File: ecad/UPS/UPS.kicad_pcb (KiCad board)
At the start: 4 copper layers, 177.8 x 139.7 mm, 162 parts, among them J1 Barrel_Jack, J2 Conn_01x02_Pin, J3 USB_C_Receptacle_USB2.0_16P, J4 PROG, J5 Conn_01x02_Pin, J6 Conn_01x02_Pin, Q1 CSD18540Q5B, Q2 Q_PMOS_DGS, Q3 IRLR7843TRPBF, Q4 Q_PMOS_DGS, Q5 CSD18540Q5B, Q6 CSD18540Q5B, Q7 CSD18540Q5B, SW3 SW_DPDT_x2, U1 BQ25730RSNR, U2 MPQ5031GRE-0001-AEC1-P, U3 L78L05_SOT89, U4 STM32L152RCT6, U5 AP2112K-3.3TRG1, U6 BOOT0, U7 NRST

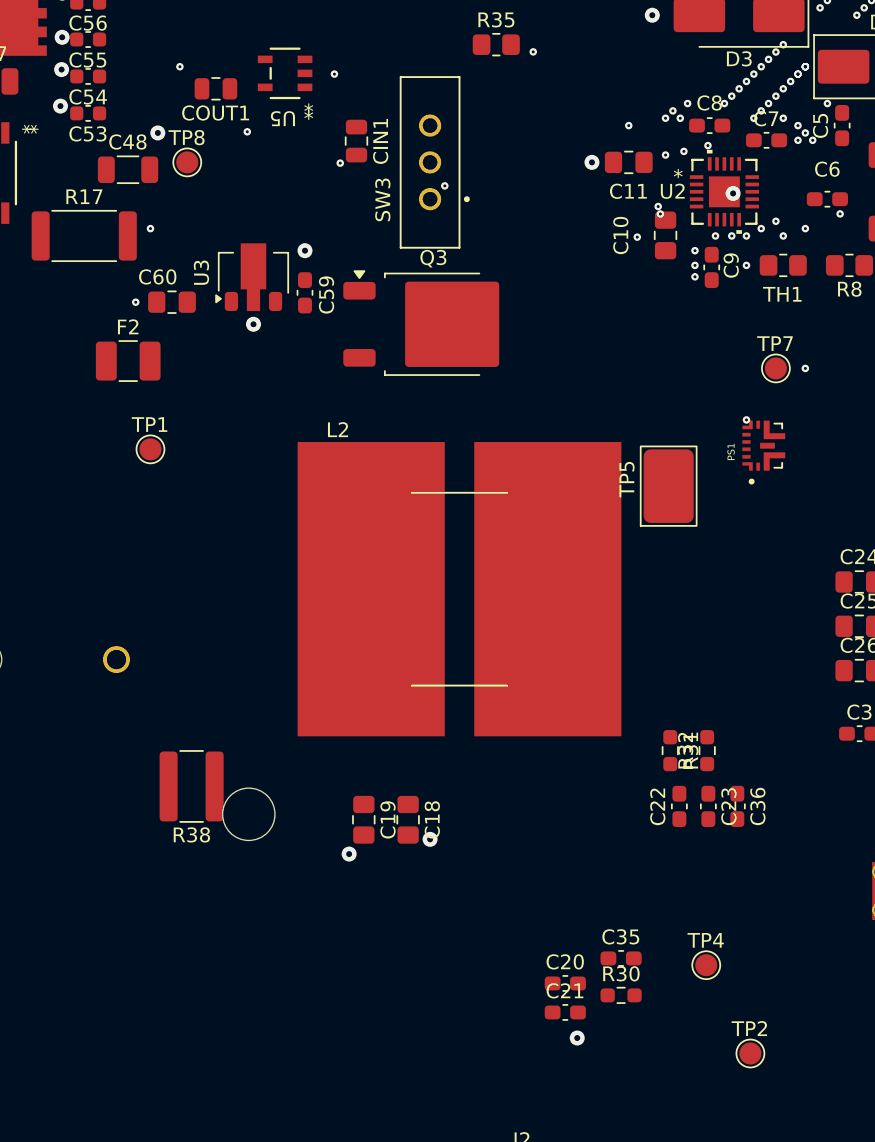
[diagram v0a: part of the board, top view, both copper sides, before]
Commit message: Final schematic, added fan, shrunk board down about 25%
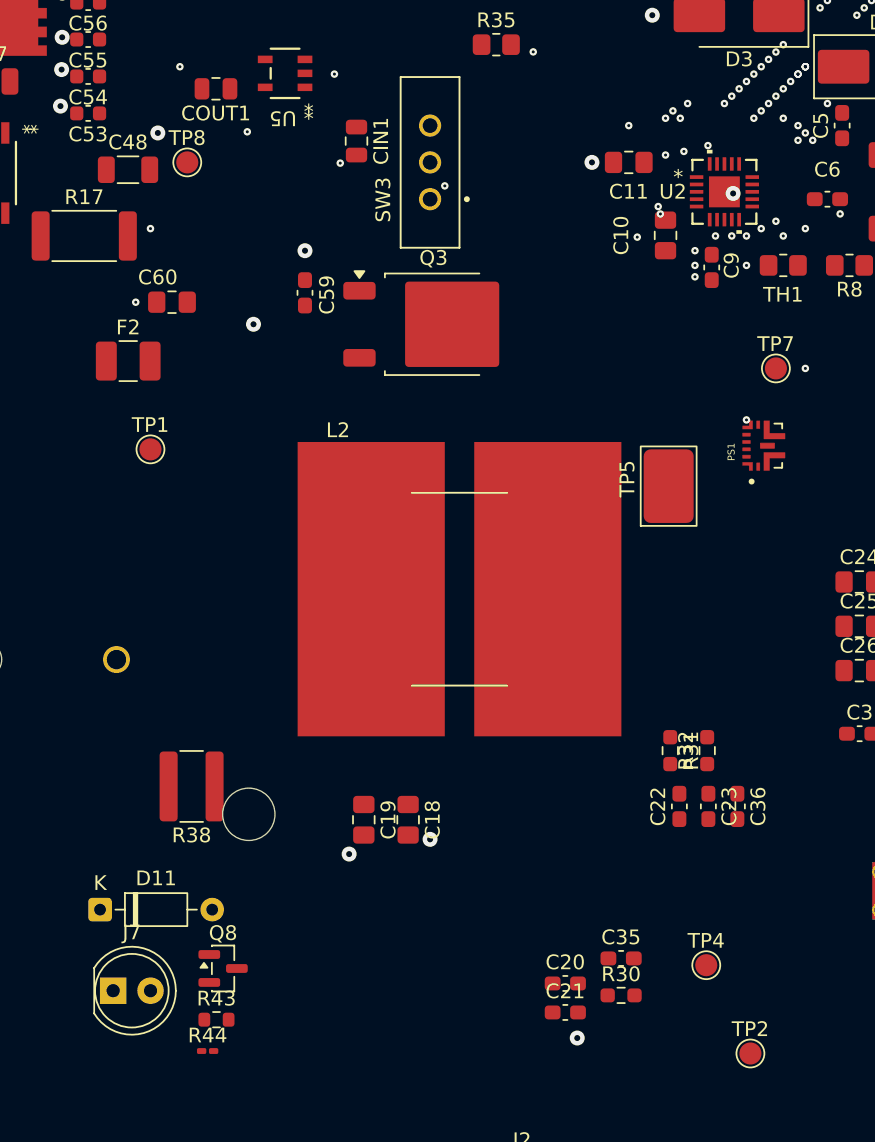
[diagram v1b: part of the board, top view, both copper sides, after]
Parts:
- removed C7, C8: 1nF, Capacitor_SMD:C_0603_1608Metric_Pad1.08x0.95mm_HandSolder
- removed U3: L78L05_SOT89, Package_TO_SOT_SMD:SOT-89-3
- added D11: 1N4148, Diode_THT:D_DO-35_SOD27_P7.62mm_Horizontal, F.Cu at (150.1, 111.8)
- added J7: Fan_Connector, LED_THT:LED_D5.0mm_IRGrey, F.Cu at (151.0, 117.3)
- added Q8: 2N7002, Package_TO_SOT_SMD:SOT-23, F.Cu at (158.4, 115.8)
- added R43: 100, Resistor_SMD:R_0603_1608Metric, F.Cu at (158.0, 119.3)
- added R44: 10K, Resistor_SMD:R_0201_0603Metric_Pad0.64x0.40mm_HandSolder, F.Cu at (157.4, 121.4)
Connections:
- C59 pad 1: /Output/VBUS_fused -> +5V
- F2 pad 2: /Output/VBUS_fused -> +5V
- Q3 pad 2: /Output/VBUS_out -> +5V
- Q3 pad 3: /Output/VBUS_fused -> /Output/VBUS_out
- U4 pad 26: unconnected-(U4B-PB0-Pad26) -> /controller/PB0
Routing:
- net PGND: vias 144 -> 148
- net Net-(U1-IADPT): vias 2 -> 1
- net NRST: vias 3 -> 1
- net GNDA: vias 11 -> 10

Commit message: ACTUALLY Shrunk board size haha
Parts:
- R40: footprint Resistor_SMD:R_0201_0603Metric_Pad0.64x0.40mm_HandSolder -> Resistor_SMD:R_0603_1608Metric_Pad0.98x0.95mm_HandSolder
- moved PS1 109.2 mm to (88.0, 101.0)
- moved L2 106.3 mm to (68.5, 82.0)
- moved C10 103.1 mm to (85.5, 70.0)
- moved C20 102.2 mm to (81.0, 99.0)
- moved U5 93.9 mm to (95.6, 120.7), turned to 0 degrees
- moved J7 85.7 mm to (65.2, 117.3)
- moved Q8 85.7 mm to (72.7, 115.8)
- moved R43 85.7 mm to (72.2, 119.3)
- moved D11 85.7 mm to (64.3, 111.8)
- moved R44 85.7 mm to (71.6, 121.4)
- moved C11 84.4 mm to (102.5, 73.0)
- moved SW3 78.8 mm to (94.5, 72.0)
- moved Q3 74.4 mm to (99.0, 82.3)
- moved C64 60.9 mm to (148.4, 116.0)
- moved R40 60.9 mm to (151.4, 114.0)
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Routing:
- net VDDA: vias 3 -> 0
- net PGND: vias 148 -> 0
- net Net-(U2-NTC): vias 2 -> 0
- net Net-(U1-SW2): vias 2 -> 0
- net Net-(U1-LODRV2): vias 2 -> 0
- net Net-(U1-IBAT): vias 2 -> 0
- net Net-(U1-IADPT): vias 1 -> 0
- net Net-(U1-ACN): vias 2 -> 0
- net Net-(SW3A-A): vias 2 -> 0
- net Net-(PS1-VIN): vias 2 -> 0
- net NRST: vias 1 -> 0
- net GNDA: vias 10 -> 0
- net COMP1: vias 1 -> 0
- net /Output/vsel2: vias 1 -> 0
- net /Output/SCL: vias 2 -> 0
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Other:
- board text added: "OSHE Pi UPS rev 2.0"
- board text removed: "OSHE Pi UPS rev 1.0"

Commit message: Started GND consolidation
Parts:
- moved C38 1.64 mm to (114.5, 85.5), turned to 90 degrees
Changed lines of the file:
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@@
 	(footprint "Capacitor_SMD:C_0603_1608Metric"
 		(layer "F.Cu")
-		(at 115.698301 84.378599)
+		(at 114.5 85.5 90)
 		(descr "Capacitor SMD 0603 (1608 Metric), square (rectangular) end terminal, IPC-7351 nominal, (Body size source: IPC-SM-782 page 76, https://www.pcb-3d.com/wordpress/wp-content/uploads/ipc-sm-782a_amendment_1_and_2.pdf), generated with kicad-footprint-generator")
 		(tags "capacitor")
 		(property "Reference" "C38"
-			(at 0 -1.43 0)
+			(at 0 -1.43 90)
 			(layer "F.SilkS")
 			(effects
@@
 		)
 		(property "Value" "1µF"
-			(at 0 1.43 0)
+			(at 0 1.43 90)
 			(layer "F.Fab")
 			(effects
@@
 		)
 		(property "Datasheet" ""
-			(at 0 0 0)
+			(at 0 0 90)
 			(layer "F.Fab")
 			(hide yes)
@@
 		)
 		(property "Description" "Unpolarized capacitor"
-			(at 0 0 0)
+			(at 0 0 90)
 			(layer "F.Fab")
 			(hide yes)
@@
 		)
 		(fp_line
+			(start 1.48 -0.73)
+			(end 1.48 0.73)
+			(stroke
+				(width 0.05)
+				(type solid)
+			)
+			(layer "F.CrtYd")
+		)
+		(fp_line
 			(start -1.48 -0.73)
 			(end 1.48 -0.73)
+			(stroke
+				(width 0.05)
+				(type solid)
+			)
+			(layer "F.CrtYd")
+		)
+		(fp_line
+			(start 1.48 0.73)
+			(end -1.48 0.73)
 			(stroke
 				(width 0.05)
@@
 		)
 		(fp_line
-			(start 1.48 -0.73)
-			(end 1.48 0.73)
+			(start 0.8 -0.4)
+			(end 0.8 0.4)
 			(stroke
-				(width 0.05)
+				(width 0.1)
 				(type solid)
 			)
-			(layer "F.CrtYd")
-		)
-		(fp_line
-			(start 1.48 0.73)
-			(end -1.48 0.73)
-			(stroke
-				(width 0.05)
-				(type solid)
-			)
-			(layer "F.CrtYd")
+			(layer "F.Fab")
 		)
 		(fp_line
 			(start -0.8 -0.4)
 			(end 0.8 -0.4)
+			(stroke
+				(width 0.1)
+				(type solid)
+			)
+			(layer "F.Fab")
+		)
+		(fp_line
+			(start 0.8 0.4)
+			(end -0.8 0.4)
 			(stroke
 				(width 0.1)
@@
 			(layer "F.Fab")
 		)
-		(fp_line
-			(start 0.8 -0.4)
-			(end 0.8 0.4)
-			(stroke
-				(width 0.1)
-				(type solid)
-			)
-			(layer "F.Fab")
-		)
-		(fp_line
-			(start 0.8 0.4)
-			(end -0.8 0.4)
-			(stroke
-				(width 0.1)
-				(type solid)
-			)
-			(layer "F.Fab")
-		)
 		(fp_text user "${REFERENCE}"
-			(at 0 0 0)
+			(at 0 0 90)
 			(layer "F.Fab")
 			(effects
@@
 		)
 		(pad "1" smd roundrect
-			(at -0.775 0)
+			(at -0.775 0 90)
 			(size 0.9 0.95)
 			(layers "F.Cu" "F.Mask" "F.Paste")
@@
 		)
 		(pad "2" smd roundrect
-			(at 0.775 0)
+			(at 0.775 0 90)
 			(size 0.9 0.95)
 			(layers "F.Cu" "F.Mask" "F.Paste")

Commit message: Update R41 Resistor from 0201 to 0603
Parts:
- R41: footprint Resistor_SMD:R_0201_0603Metric_Pad0.64x0.40mm_HandSolder -> Resistor_SMD:R_0603_1608Metric_Pad0.98x0.95mm_HandSolder
- TP3: value PGNDTest -> GNDTest
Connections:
- B1 pad 1: PGND -> GND
- B2 pad 1: PGND -> GND
- B3 pad 1: PGND -> GND
- B4 pad 1: PGND -> GND
- C1 pad 2: GNDA -> GND
- C10 pad 2: PGND -> GND
- C11 pad 1: PGND -> GND
- C12 pad 2: PGND -> GND
- C13 pad 2: PGND -> GND
- C15 pad 1: PGND -> GND
- C18 pad 2: PGND -> GND
- C19 pad 2: PGND -> GND
- C2 pad 2: GNDA -> GND
- C21 pad 2: PGND -> GND
- C23 pad 2: AGND -> GND
- C24 pad 2: PGND -> GND
- C25 pad 2: PGND -> GND
- C26 pad 2: PGND -> GND
- C27 pad 1: PGND -> GND
- C28 pad 1: GNDA -> GND
- C29 pad 1: GNDA -> GND
- C3 pad 2: PGND -> GND
- C30 pad 1: GNDA -> GND
- C31 pad 1: GNDA -> GND
- C33 pad 2: PGND -> GND
- C34 pad 2: PGND -> GND
- C35 pad 2: AGND -> GND
- C36 pad 2: AGND -> GND
- C37 pad 2: PGND -> GND
- C38 pad 2: GNDA -> GND
- C39 pad 2: PGND -> GND
- C4 pad 2: PGND -> GND
- C40 pad 2: PGND -> GND
- C41 pad 2: PGND -> GND
- C42 pad 2: PGND -> GND
- C43 pad 2: PGND -> GND
- C44 pad 2: PGND -> GND
- C45 pad 2: PGND -> GND
- C46 pad 2: PGND -> GND
- C47 pad 2: PGND -> GND
- C48 pad 2: PGND -> GND
- C49 pad 1: PGND -> GND
- C5 pad 2: PGND -> GND
- C50 pad 1: PGND -> GND
- C51 pad 2: PGND -> GND
- C52 pad 2: PGND -> GND
- C53 pad 2: PGND -> GND
- C54 pad 2: PGND -> GND
- C55 pad 2: PGND -> GND
- C56 pad 2: PGND -> GND
- C57 pad 2: PGND -> GND
- C58 pad 2: PGND -> GND
- C59 pad 2: PGND -> GND
- C6 pad 2: PGND -> GND
- C60 pad 1: PGND -> GND
- C62 pad 1: PGND -> GND
- C63 pad 1: PGND -> GND
- C64 pad 2: PGND -> GND
- C68 pad 2: GNDA -> GND
- C69 pad 2: GNDA -> GND
- C70 pad 2: GNDA -> GND
- C9 pad 2: PGND -> GND
- CIN1 pad 2: PGND -> GND
- COUT1 pad 2: PGND -> GND
- D1 pad 2: PGND -> GND
- D2 pad 2: PGND -> GND
- D3 pad 2: PGND -> GND
- D4 pad 2: PGND -> GND
- D5 pad 2: PGND -> GND
- J1 pad 2: PGND -> GND
- J2 pad 2: GNDA -> GND
- J3 pad A1: PGND -> GND
- J3 pad A12: PGND -> GND
- J3 pad B1: PGND -> GND
- J3 pad B12: PGND -> GND
- J3 pad S1: PGND -> GND
- J4 pad 4: PGND -> GND
- J5 pad 2: GNDA -> GND
- J6 pad 2: GNDA -> GND
- NT1 pad 1: AGND -> GND
- NT1 pad 2: PGND -> GND
- NT1 pad 3: PGND -> GND
- PS1 pad 10: AGND -> GND
- PS1 pad 3: PGND -> GND
- Q5 pad 1: PGND -> GND
- Q5 pad 2: PGND -> GND
- Q5 pad 3: PGND -> GND
- Q6 pad 1: PGND -> GND
- Q6 pad 2: PGND -> GND
- Q6 pad 3: PGND -> GND
- Q7 pad 4: PGND -> GND
- Q8 pad 2: PGND -> GND
- R1 pad 2: GNDA -> GND
- R18 pad 2: PGND -> GND
- R2 pad 2: GNDA -> GND
- R20 pad 2: PGND -> GND
- R21 pad 2: PGND -> GND
- R22 pad 2: PGND -> GND
- R23 pad 1: PGND -> GND
- R27 pad 1: PGND -> GND
- R3 pad 2: GNDA -> GND
- R30 pad 2: AGND -> GND
- R31 pad 2: AGND -> GND
- R33 pad 2: PGND -> GND
- R35 pad 2: PGND -> GND
- R41 pad 2: PGND -> GND
- R44 pad 1: PGND -> GND
- TH1 pad 2: PGND -> GND
- TP2 pad 1: AGND -> GND
- TP3 pad 1: PGND -> GND
- U1 pad 27: PGND -> GND
- U1 pad 31: PGND -> GND
- U1 pad 33: PGND -> GND
- U2 pad 10: PGND -> GND
- U2 pad 21: PGND -> GND
- U2 pad 8: PGND -> GND
- U4 pad 12: PGND -> GND
- U4 pad 18: PGND -> GND
- U4 pad 31: PGND -> GND
- U4 pad 47: PGND -> GND
- U4 pad 63: PGND -> GND
- U5 pad 2: PGND -> GND
- U7 pad 2: PGND -> GND
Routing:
- added copper zone on In1.Cu, net GND
- removed copper zone on In1.Cu, net PGND

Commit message: Light PCB work
Also removed NetTie
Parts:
- removed NT1: NetTie_3, NetTie:NetTie-4_THT_Pad1.0mm
- R44: footprint Resistor_SMD:R_0201_0603Metric_Pad0.64x0.40mm_HandSolder -> Resistor_SMD:R_0603_1608Metric_Pad0.98x0.95mm_HandSolder
- moved J6 38.6 mm to (99.0, 145.0)
- moved R34 36.1 mm to (103.5, 138.5)
- moved R18 29.5 mm to (91.5, 139.5), turned to -90 degrees
- moved R8 27.1 mm to (137.0, 118.0)
- moved R19 24.1 mm to (87.5, 136.0)
- moved J1 16.4 mm to (64.5, 47.0)
- moved D2 16.3 mm to (162.0, 113.7), turned to 90 degrees
- moved R24 15.6 mm to (71.7, 136.4)
- moved R28 15.6 mm to (98.7, 135.9)
- moved C27 15.6 mm to (68.2, 156.8)
- moved C4 15.6 mm to (110.9, 151.0)
- moved C49 15.6 mm to (80.7, 154.3)
- moved C50 15.6 mm to (64.7, 146.2)
- moved C61 15.6 mm to (79.0, 136.8)
- moved C62 15.6 mm to (67.3, 140.8)
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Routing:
- net GND: track 0.00 -> 23.7 mm, vias 0 -> 9
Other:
- board size 177.8 x 139.7 mm -> 121.9 x 139.7 mm

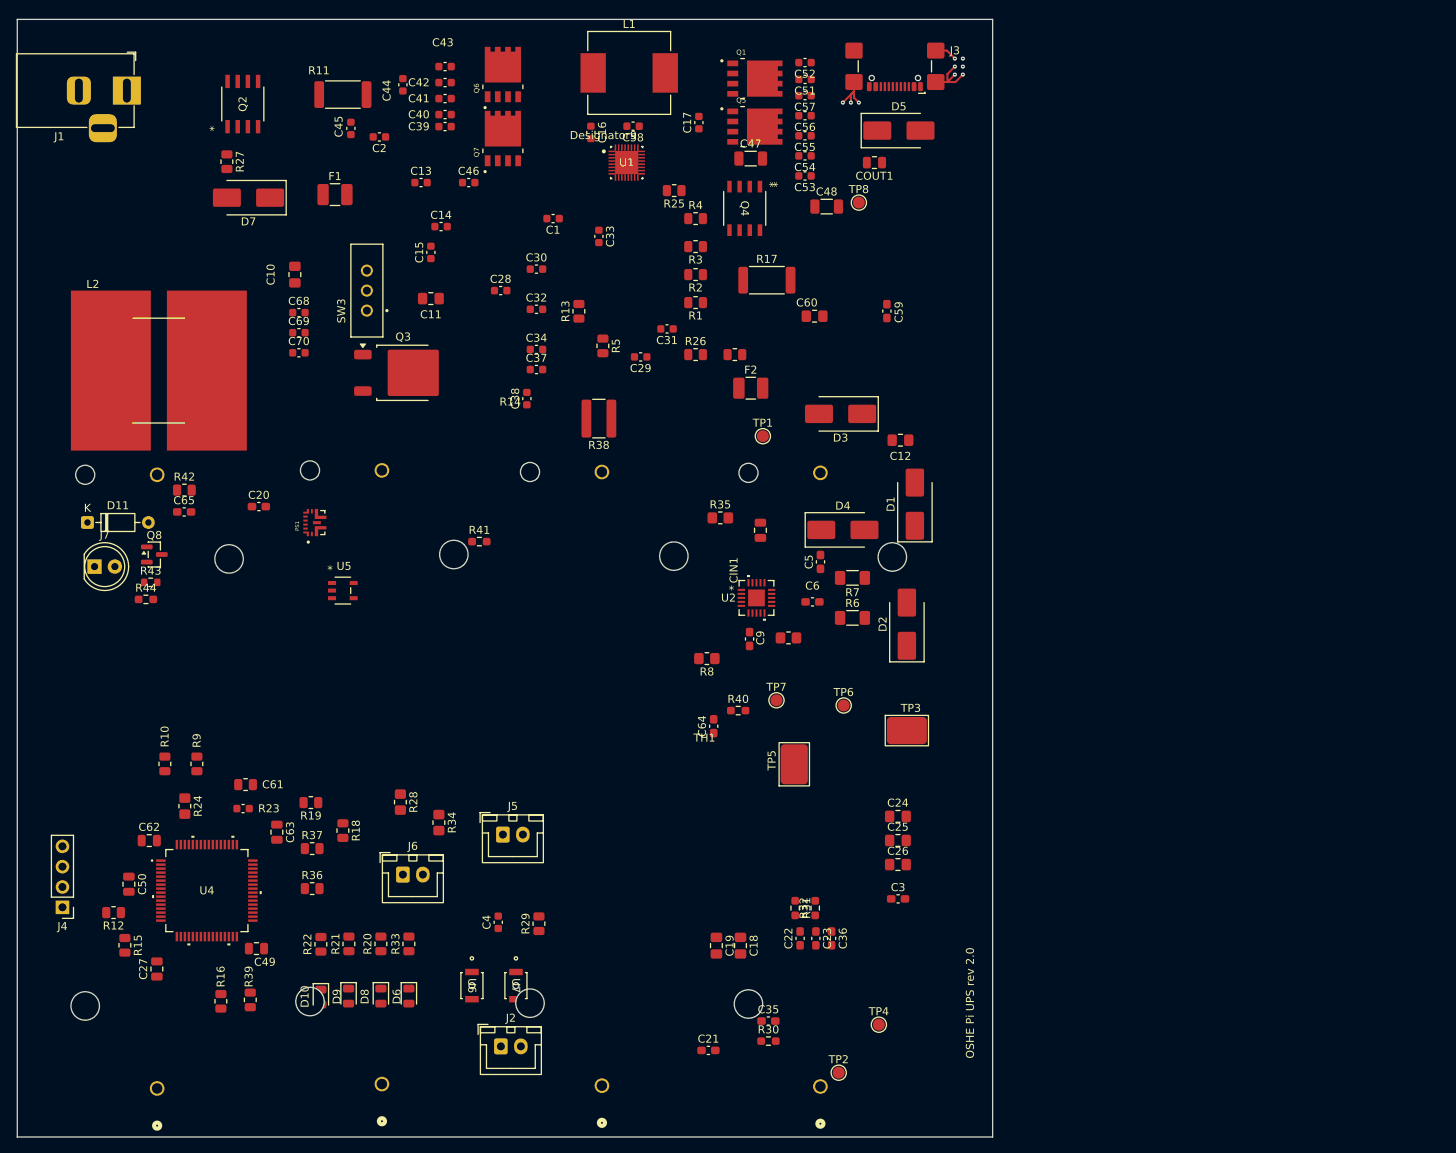
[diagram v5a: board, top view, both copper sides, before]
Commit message: Little routing, also fixed barrel jack to match input
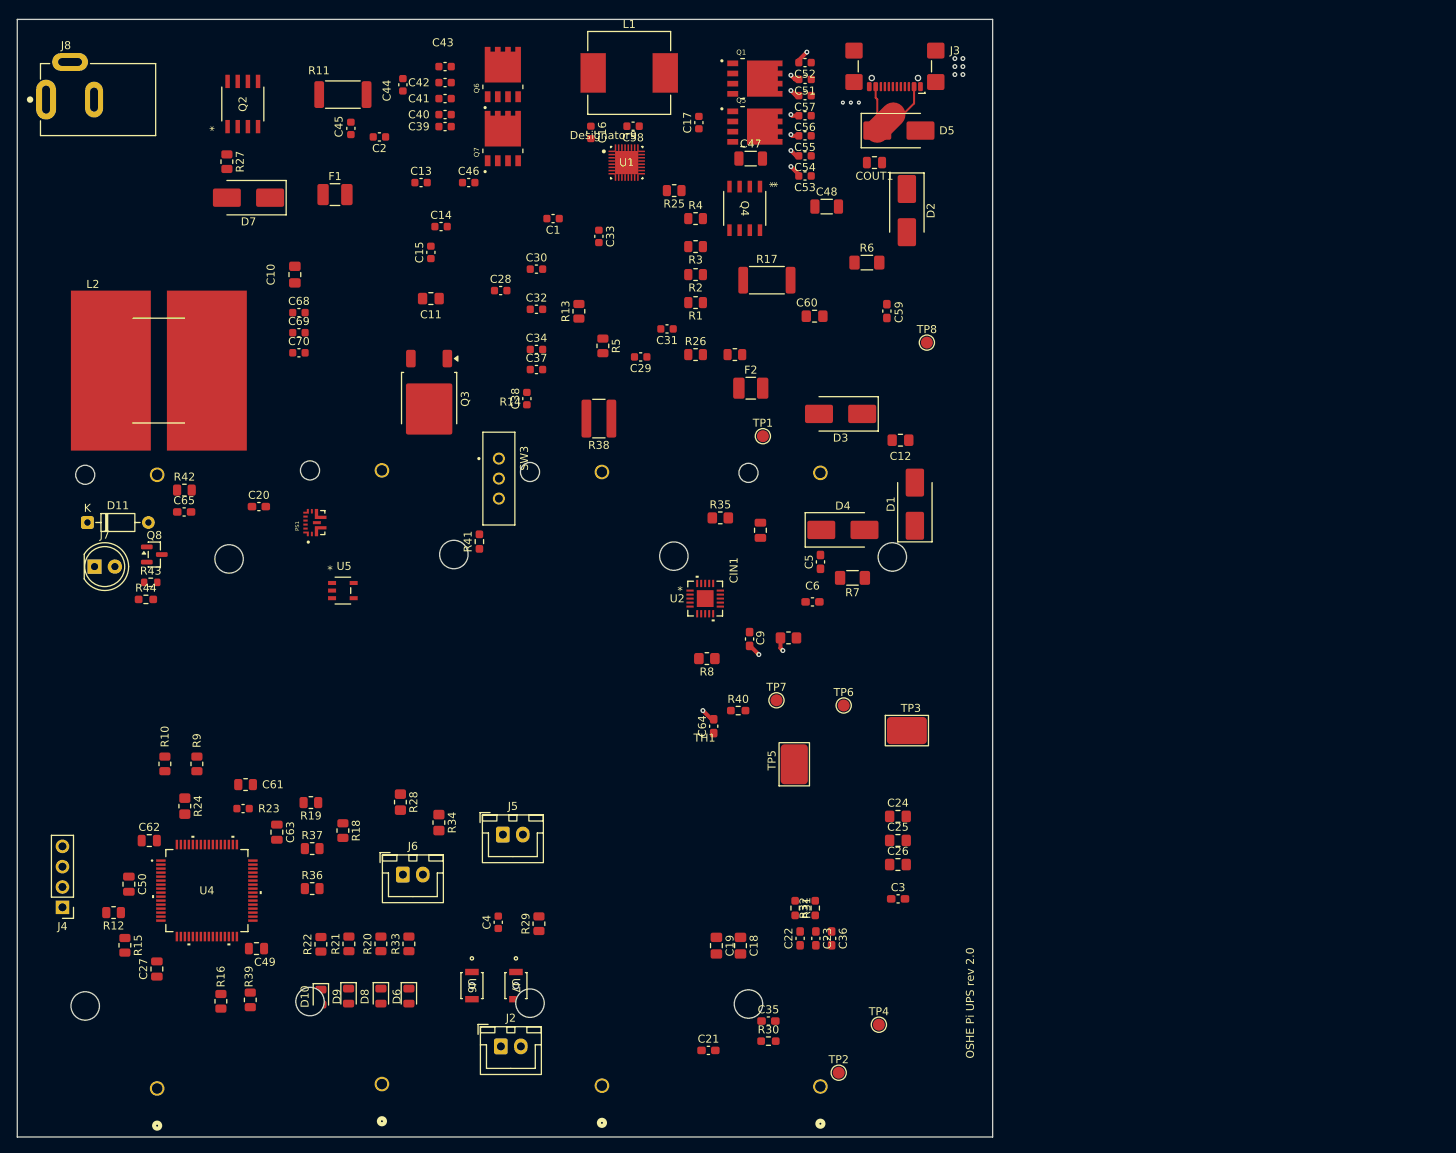
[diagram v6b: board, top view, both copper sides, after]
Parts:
- removed J1: Barrel_Jack, Connector_BarrelJack:BarrelJack_Horizontal
- added J8: PJ-002AH, PJ-002AH:CUI_PJ-002AH, F.Cu at (54.4, 48.1)
- moved D2 51.7 mm to (162.0, 62.0), turned to -90 degrees
- moved R6 44.4 mm to (157.0, 68.5)
- moved SW3 28.7 mm to (111.0, 95.5), turned to -90 degrees
- moved TP8 19.5 mm to (164.5, 78.5)
- moved U2 6.41 mm to (136.8, 110.5)
- moved Q3 4.60 mm to (102.3, 85.5), turned to -90 degrees
- turned R41 to 90 degrees
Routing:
- net /Output/VBUS_out: track 0.00 -> 13.7 mm
- net GND: track 23.7 -> 20.3 mm, vias 9 -> 19

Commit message: First real successful copper pour, some charger routing too
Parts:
- moved TP3 106.0 mm to (57.0, 114.9)
- moved C25 84.8 mm to (92.5, 90.5)
- moved C26 84.8 mm to (92.5, 93.5)
- moved C3 84.8 mm to (92.5, 97.8)
- moved C24 84.8 mm to (92.5, 87.5)
- moved C21 57.5 mm to (106.2, 118.5)
- moved C35 52.5 mm to (129.6, 113.0)
- moved R30 52.5 mm to (129.6, 115.5)
- moved R31 51.6 mm to (117.0, 107.9)
- moved TP4 51.6 mm to (127.5, 122.5)
- moved C19 51.6 mm to (107.2, 112.6)
- moved C22 51.6 mm to (117.7, 111.7)
- moved C23 51.6 mm to (119.6, 111.7)
- moved C36 51.6 mm to (121.6, 111.7)
- moved R32 51.6 mm to (119.5, 107.9)
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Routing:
- net Net-(U1-LODRV1): track 0.00 -> 34.0 mm
- net Net-(U1-ACN): track 0.00 -> 13.6 mm
- added copper zone on F.Cu, net /Charger/Charger_VBUS_IN
